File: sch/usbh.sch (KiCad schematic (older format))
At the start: 2 parts, among them IC6 MAX3421EEHJ+, U1 PCMCIA_BOARD

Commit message: Add voltage regulator
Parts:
- IC6: footprint QFP50P700X700X120-32N -> MAX3421EEHJ+:QFP50P700X700X120-32N
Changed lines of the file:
@@
 $Descr A4 11693 8268
 encoding utf-8
-Sheet 3 4
+Sheet 4 4
 Title ""
 Date ""
@@
 F 0 "IC6" H 6544 3596 50  0000 L CNN
 F 1 "MAX3421EEHJ+" H 6544 3505 50  0000 L CNN
-F 2 "QFP50P700X700X120-32N" H 6350 4400 50  0001 L CNN
+F 2 "MAX3421EEHJ+:QFP50P700X700X120-32N" H 6350 4400 50  0001 L CNN
 F 3 "http://docs-emea.rs-online.com/webdocs/0f71/0900766b80f71b08.pdf" H 6350 4300 50  0001 L CNN
 F 4 "MAX3421EEHJ+, USB Controller 12 Mbit/s USB 2.0, 3.3 V, 32-Pin, TQFP" H 6350 4200 50  0001 L CNN "Description"

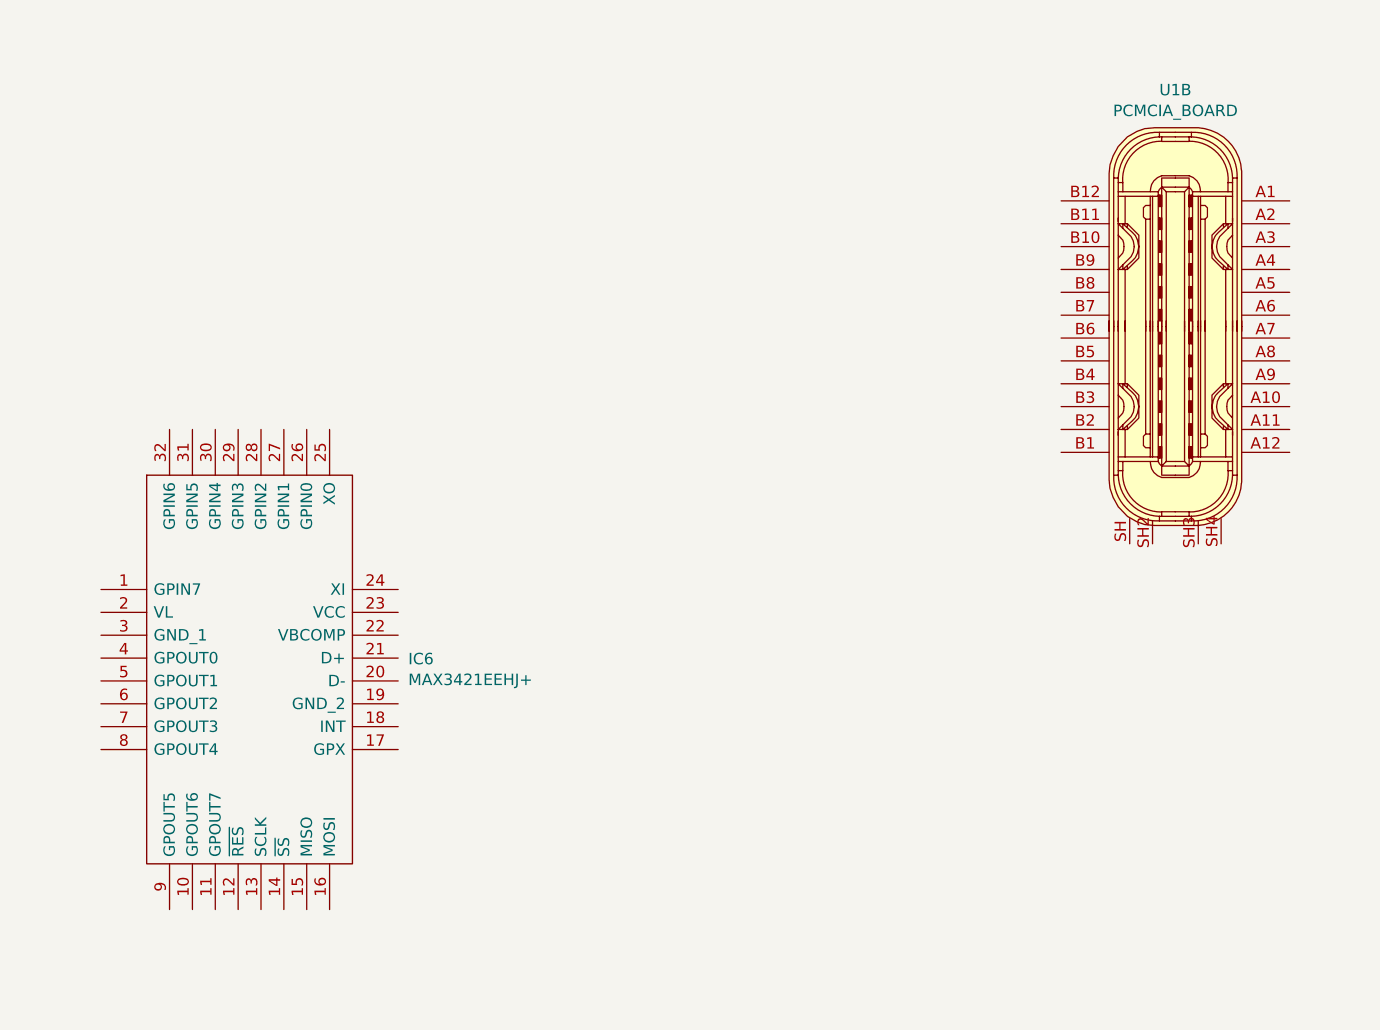
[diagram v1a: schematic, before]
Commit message: Add usb controller
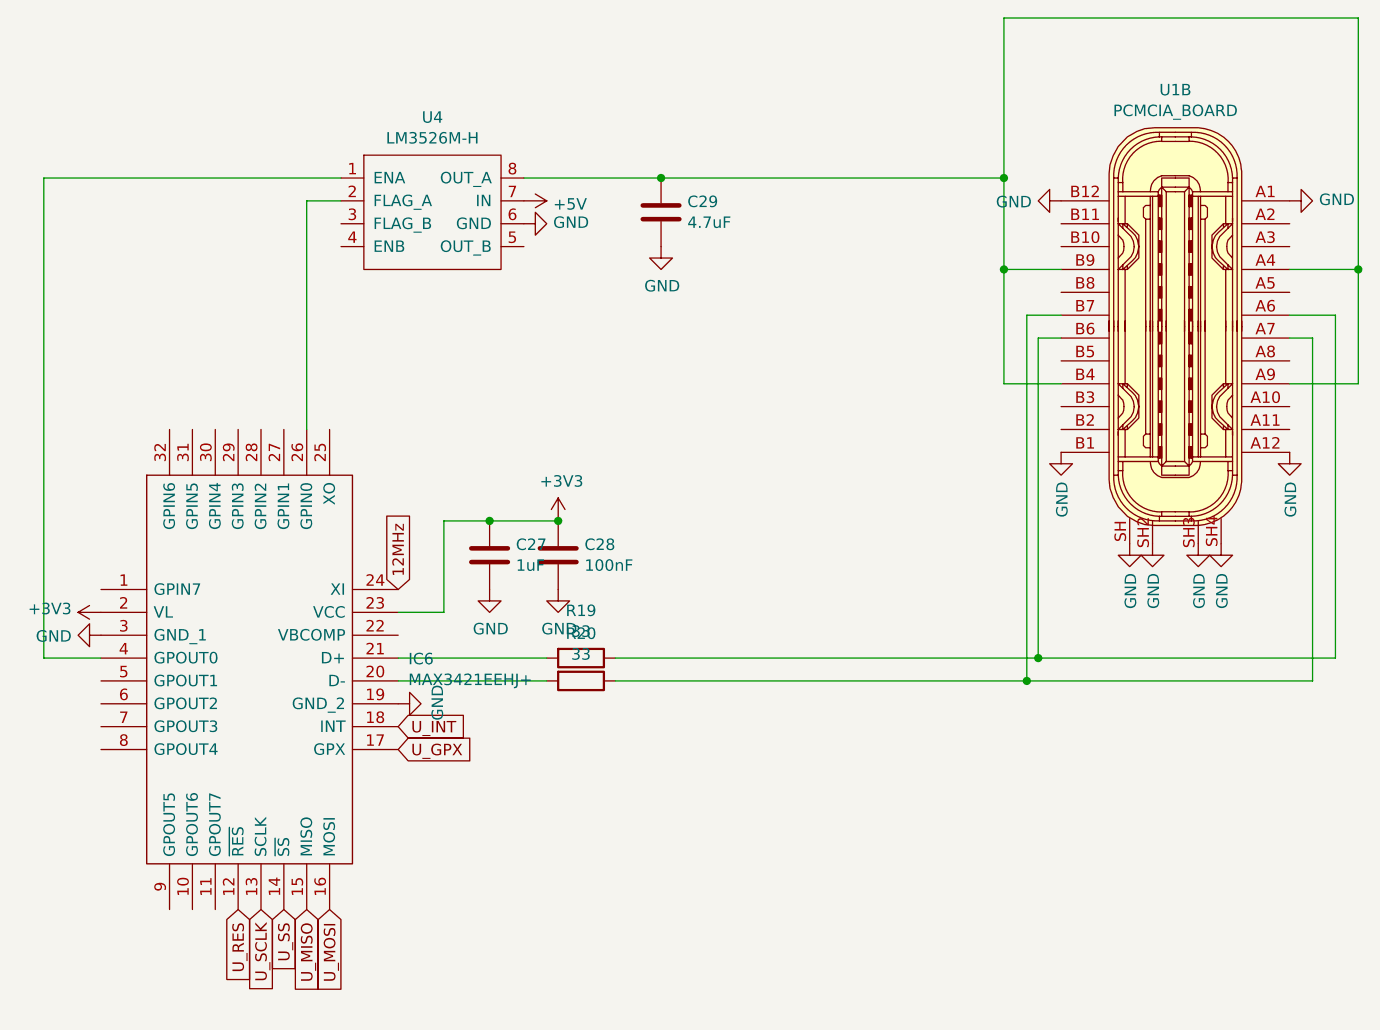
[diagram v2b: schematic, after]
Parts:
- added C27: 1uF, Capacitor_SMD:C_0805_2012Metric, symbol Device:C
- added C28: 100nF, Capacitor_SMD:C_0402_1005Metric, symbol Device:C
- added C29: 4.7uF, Capacitor_SMD:C_0805_2012Metric, symbol Device:C
- added R19, R20: 33, Resistor_SMD:R_0402_1005Metric, symbol Device:R
- added U4: LM3526M-H, Package_SO:SOIC-8_3.9x4.9mm_P1.27mm, symbol LM3526M:LM3526M-H
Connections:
- net GND: now reaches U1.A1
- net GND: now also IC6.19 (GND_2), IC6.3 (GND_1), U1.A12, U1.B1, U1.B12, U1.SH, U1.SH2, U1.SH3, U1.SH4, C27.2, C28.2, C29.2, U4.6 (GND)
- net at U1.A4: now also U1.A9, U1.B4, U1.B9, C29.1, U4.8 (OUT_A)
- net at U1.A6: now also U1.B6, R19.1
- net at U1.A7: now also U1.B7, R20.1
- net U_RES: now reaches IC6.12 (~RES)
- net U_SCLK: now reaches IC6.13 (SCLK)
- net U_SS: now reaches IC6.14 (~SS)
- net U_MISO: now reaches IC6.15 (MISO)
- net U_MOSI: now reaches IC6.16 (MOSI)
- net U_GPX: now reaches IC6.17 (GPX)
- net U_INT: now reaches IC6.18 (INT)
- net +3V3: now reaches IC6.2 (VL)
- net +3V3: now also IC6.23 (VCC), C27.1, C28.1
- net at IC6.20 (D-): now also R20.2
- net at IC6.21 (D+): now also R19.2
- net 12MHz: now reaches IC6.24 (XI)
- net at IC6.26 (GPIN0): now also U4.2 (FLAG_A)
- net at IC6.4 (GPOUT0): now also U4.1 (ENA)
- new net +5V: U4.7 (IN)

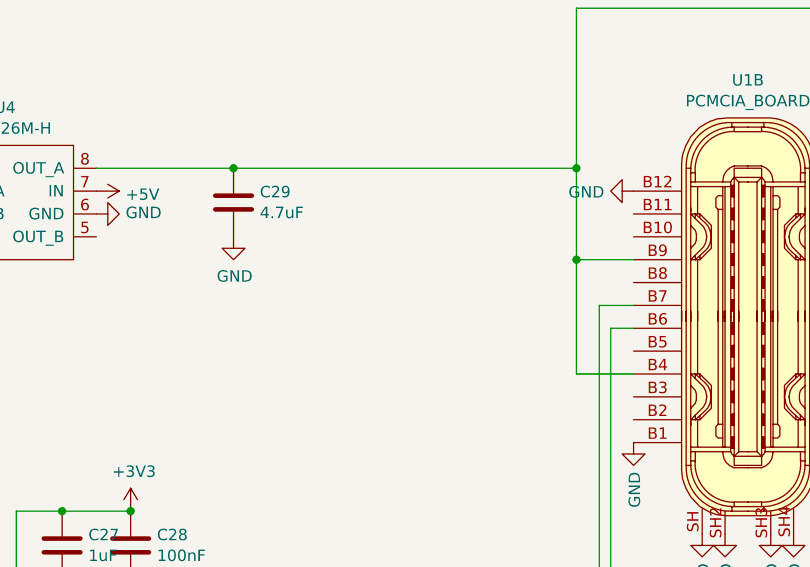
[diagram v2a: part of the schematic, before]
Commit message: Add power led
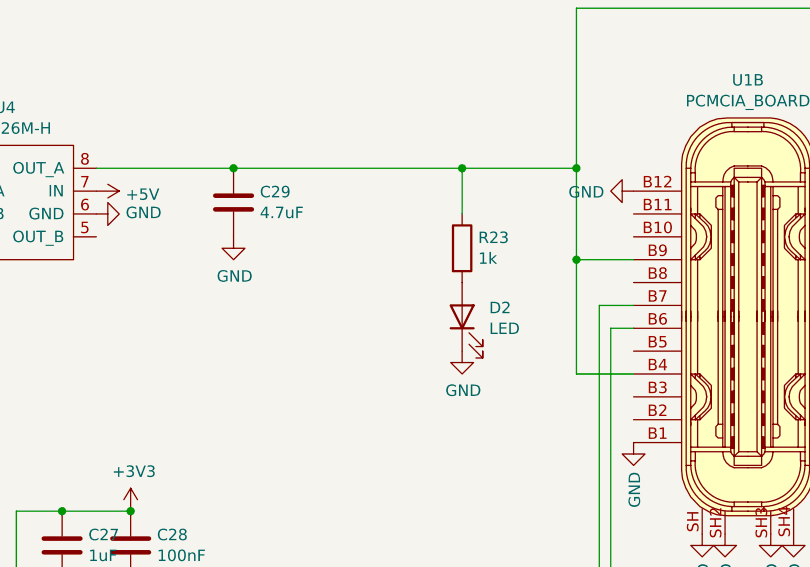
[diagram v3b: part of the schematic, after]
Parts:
- added D2: LED, LED_SMD:LED_PLCC-2, symbol Device:LED
- added R23: 1k, Resistor_SMD:R_0402_1005Metric, symbol Device:R
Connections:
- net GND: now also D2.1 (K)
- net at C29.1, U1.A4, U1.A9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: now also R23.1
- new net: D2.2 (A), R23.2
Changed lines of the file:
@@
 	7050 2100 7650 2100
 Wire Wire Line
-	7650 2100 9150 2100
+	7650 2100 8650 2100
 Wire Wire Line
 	9150 2100 9150 2500
@@
 	1    0    0    -1
 $EndComp
+$Comp
+L Device:LED D2
+U 1 1 6083075E
+P 8650 2750
+F 0 "D2" V 8689 2632 50  0000 R CNN
+F 1 "LED" V 8598 2632 50  0000 R CNN
+F 2 "LED_SMD:LED_PLCC-2" H 8650 2750 50  0001 C CNN
+F 3 "~" H 8650 2750 50  0001 C CNN
+	1    8650 2750
+	0    -1   -1   0
+$EndComp
+$Comp
+L power:GND #PWR0198
+U 1 1 608313B9
+P 8650 2900
+F 0 "#PWR0198" H 8650 2650 50  0001 C CNN
+F 1 "GND" H 8655 2727 50  0000 C CNN
+F 2 "" H 8650 2900 50  0001 C CNN
+F 3 "" H 8650 2900 50  0001 C CNN
+	1    8650 2900
+	1    0    0    -1
+$EndComp
+$Comp
+L Device:R R23
+U 1 1 60831EAD
+P 8650 2450
+F 0 "R23" H 8720 2496 50  0000 L CNN
+F 1 "1k" H 8720 2405 50  0000 L CNN
+F 2 "Resistor_SMD:R_0402_1005Metric" V 8580 2450 50  0001 C CNN
+F 3 "~" H 8650 2450 50  0001 C CNN
+	1    8650 2450
+	1    0    0    -1
+$EndComp
+Wire Wire Line
+	8650 2300 8650 2100
+Connection ~ 8650 2100
+Wire Wire Line
+	8650 2100 9150 2100
 $EndSCHEMATC

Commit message: Add Connector
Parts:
- D2: footprint LED_SMD:LED_PLCC-2 -> LED_SMD:LED_0603_1608Metric
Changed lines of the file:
@@
 U 1 1 60EF6966
 P 6650 2650
-AR Path="/60EF6966" Ref="U4"  Part="1"
-AR Path="/60E07D1B/60EF6966" Ref="U4"  Part="1"
 F 0 "U4" H 6650 3465 50  0000 C CNN
 F 1 "LM3526M-H" H 6650 3374 50  0000 C CNN
@@
 F 0 "D2" V 8689 2632 50  0000 R CNN
 F 1 "LED" V 8598 2632 50  0000 R CNN
-F 2 "LED_SMD:LED_PLCC-2" H 8650 2750 50  0001 C CNN
+F 2 "LED_SMD:LED_0603_1608Metric" H 8650 2750 50  0001 C CNN
 F 3 "~" H 8650 2750 50  0001 C CNN
 	1    8650 2750

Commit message: V2.0 board
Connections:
- net at C29.1, R23.1, U1.A4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: now also IC6.22 (VBCOMP)
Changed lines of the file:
@@
 	7050 2100 7650 2100
 Wire Wire Line
-	7650 2100 8650 2100
+	7650 2100 8050 2100
 Wire Wire Line
 	9150 2100 9150 2500
@@
 Wire Wire Line
 	8650 2100 9150 2100
+Wire Wire Line
+	6500 4100 8050 4100
+Wire Wire Line
+	8050 4100 8050 2100
+Connection ~ 8050 2100
+Wire Wire Line
+	8050 2100 8650 2100
 $EndSCHEMATC
